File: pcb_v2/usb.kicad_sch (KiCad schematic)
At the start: 13 parts, among them J3 USB_C_ReceptacleUSB2.0, J4 Conn_01x03_Socket, U2 AMS1117-3.3

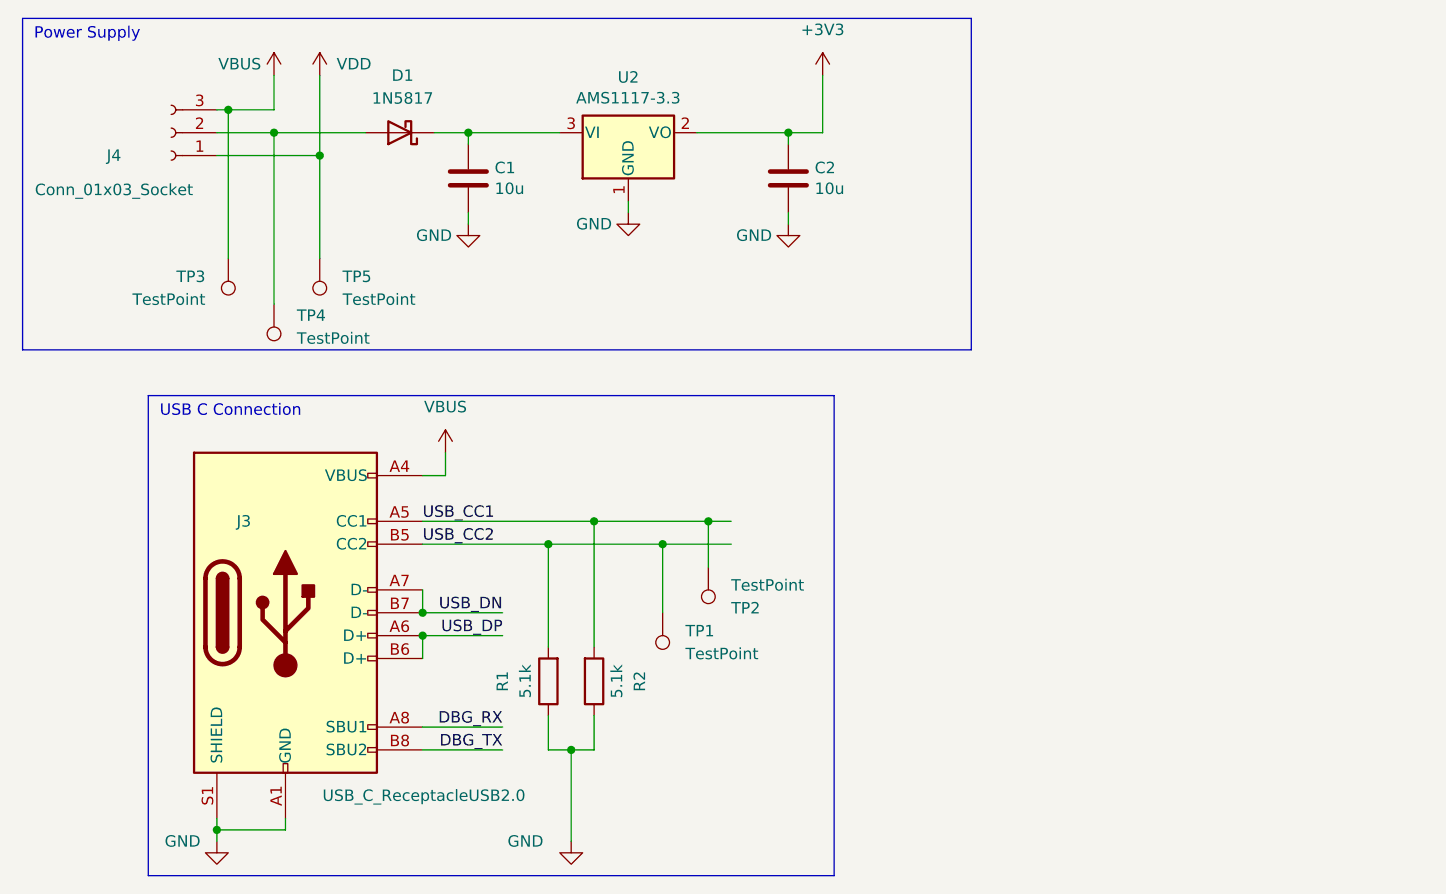
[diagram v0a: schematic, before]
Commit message: Connect pin sheets. Add protection on USB. Use SolderJumpers.
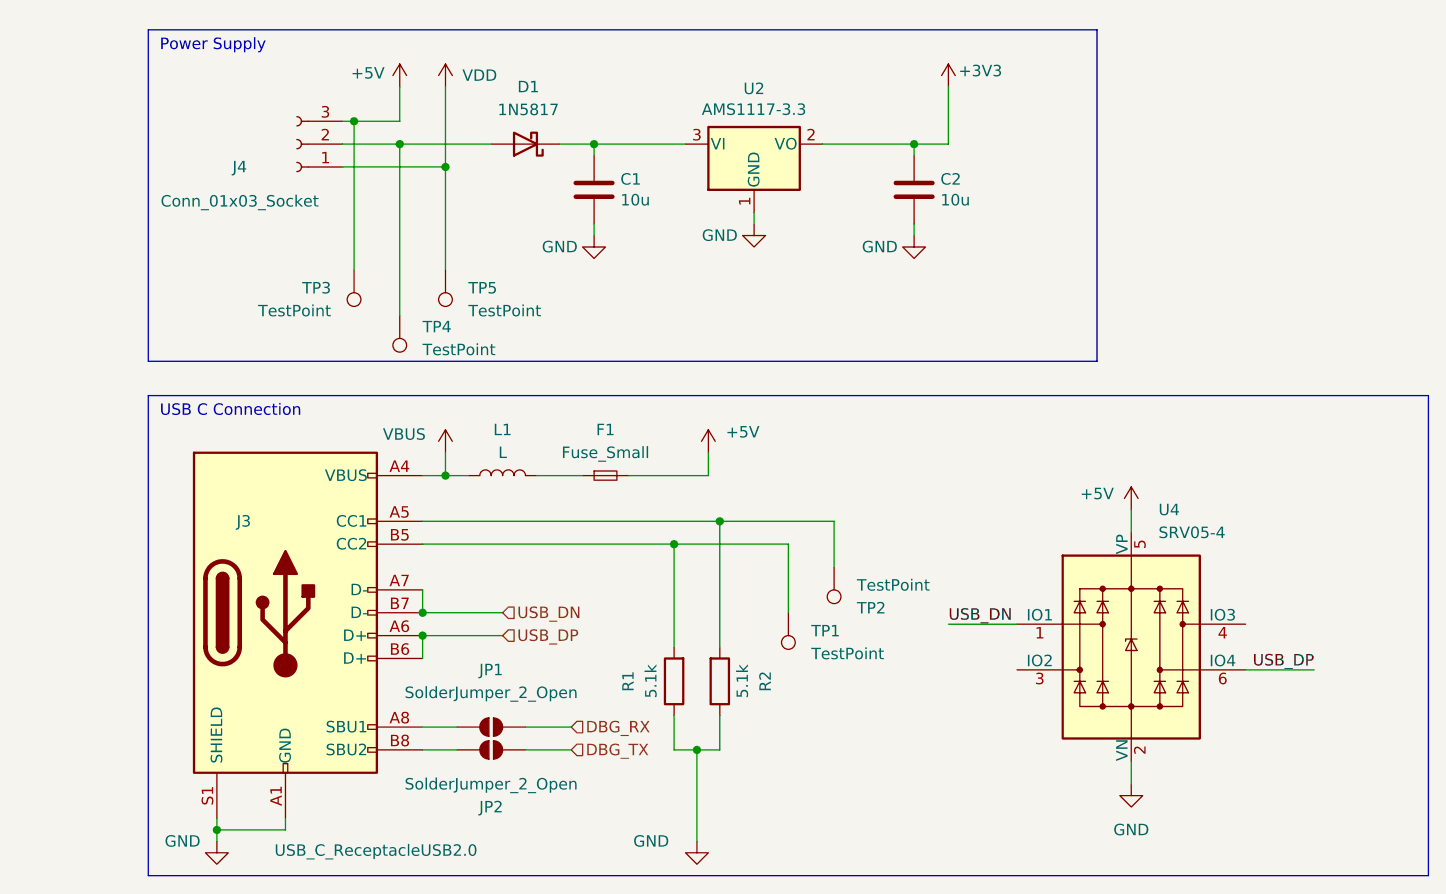
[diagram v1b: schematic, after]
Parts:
- added F1: Fuse_Small, symbol Device:Fuse_Small
- added JP1, JP2: SolderJumper_2_Open, symbol Jumper:SolderJumper_2_Open
- added L1: L, symbol Device:L
- added U4: SRV05-4, Package_TO_SOT_SMD:SOT-23-6, symbol Power_Protection:SRV05-4
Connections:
- net DBG_RX: now also JP1.2 (B); no longer J3.A8 (SBU1)
- net DBG_TX: now also JP2.1 (A); no longer J3.B8 (SBU2)
- net GND: now also U4.2 (VN)
- net USB_DN: now also U4.1 (IO1)
- net USB_DP: now also U4.6 (IO4)
- net VBUS: now also L1.1; no longer J4.3 (Pin_3), TP3.1
- net USB_CC1: no longer names the net of J3.A5 (CC1), R2.2, TP2.1
- net USB_CC2: no longer names the net of J3.B5 (CC2), R1.2, TP1.1
- new net: F1.1, L1.2
- new net: J3.A8 (SBU1), JP1.1 (A)
- new net: J3.B8 (SBU2), JP2.2 (B)
- new net +5V: F1.2, J4.3 (Pin_3), TP3.1, U4.5 (VP)
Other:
- moved on the sheet: C1, C2, D1, J4, R1, R2, TP1, TP2, TP3, TP4, TP5, U2
